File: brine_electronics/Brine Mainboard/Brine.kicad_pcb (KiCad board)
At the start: 2 copper layers, 30.5 x 42.7 mm, 17 parts, among them J1 Conn_01x02_Socket, U1 XIAO-ESP32-S3-SMD, U2 VL53L1CXV0FY1

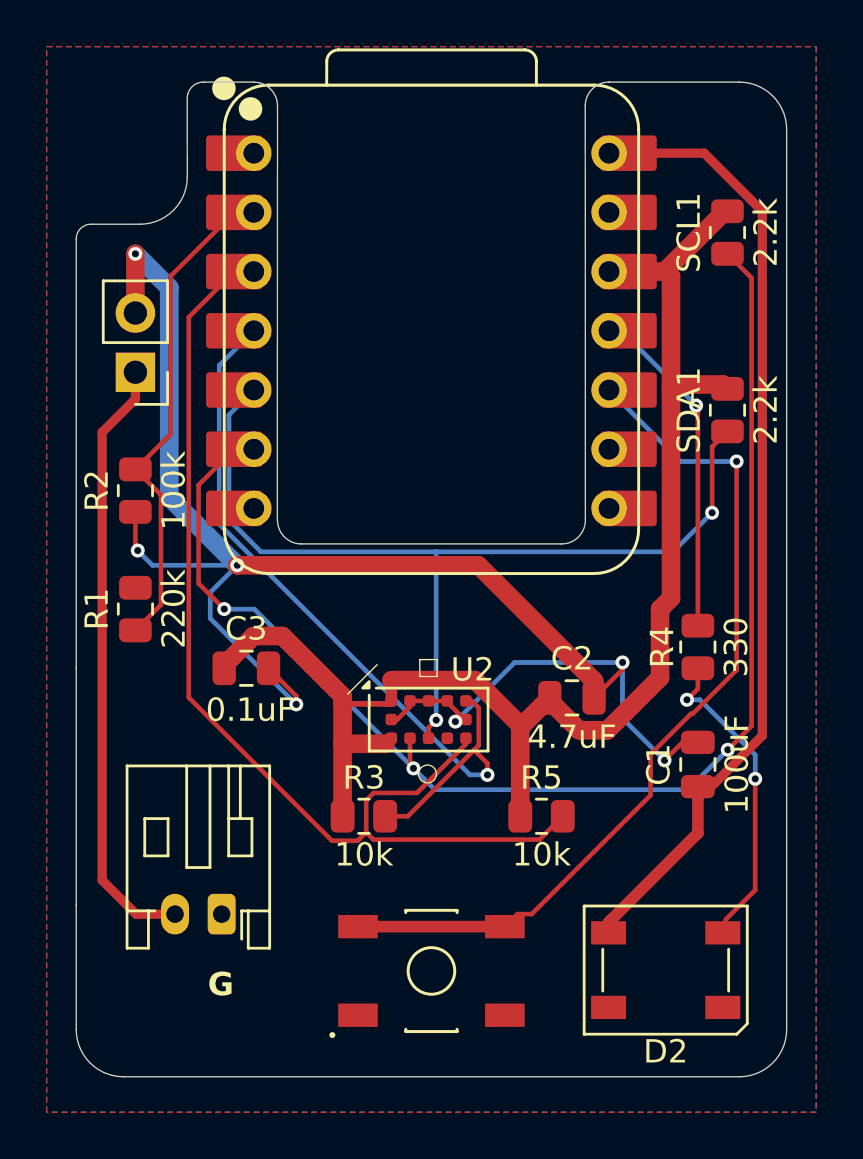
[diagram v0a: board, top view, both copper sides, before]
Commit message: Resolved DRC errors ✅
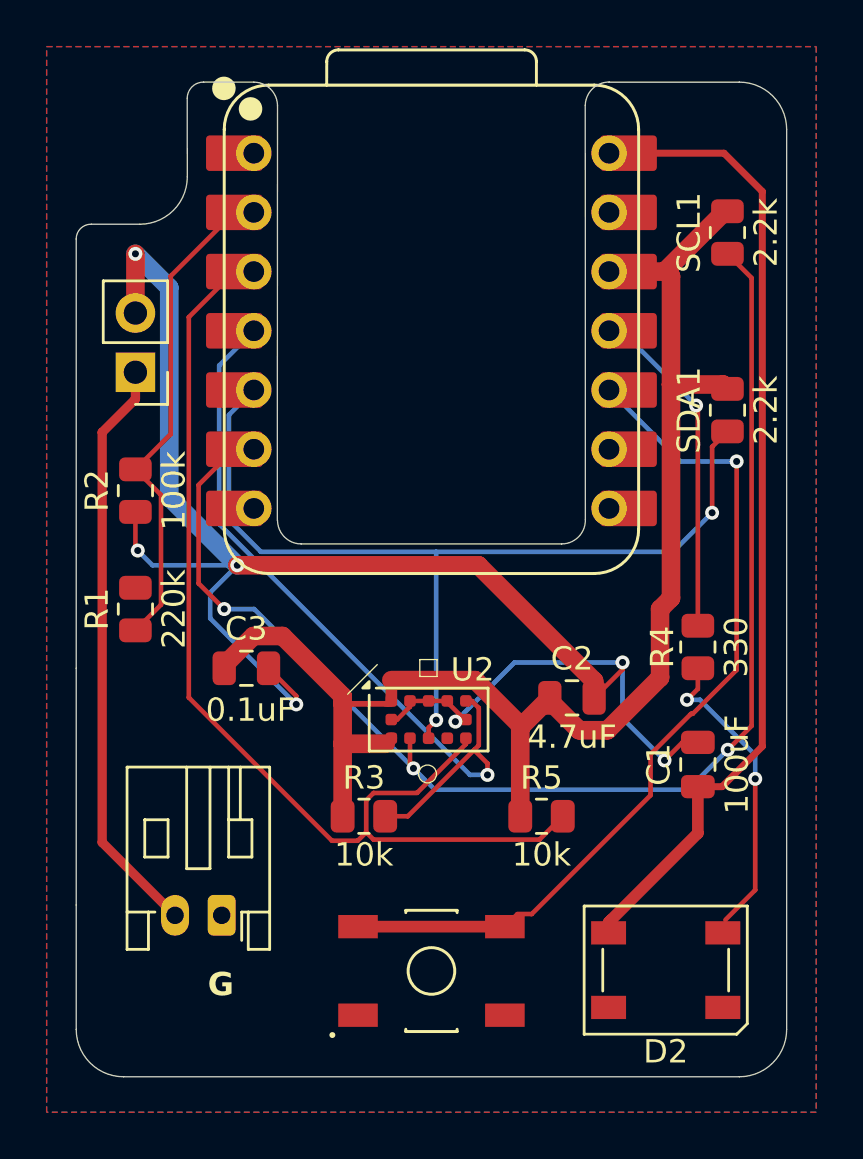
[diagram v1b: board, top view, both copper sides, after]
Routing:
- net /Battery/BATT: track 26.1 -> 25.2 mm
- net +5V: track 41.6 -> 42.4 mm
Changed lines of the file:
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@@
 	(footprint "Connector_JST:JST_PH_S2B-PH-K_1x02_P2.00mm_Horizontal"
 		(layer "F.Cu")
-		(at 143.4 105.8 180)
+		(at 143.4 105.85 180)
 		(descr "JST PH series connector, S2B-PH-K (http://www.jst-mfg.com/product/pdf/eng/ePH.pdf), generated with kicad-footprint-generator")
 		(tags "connector JST PH horizontal")
@@
 	)
 	(segment
-		(start 166.5954 98.1391)
-		(end 164.4045 100.33)
-		(width 0.4)
+		(start 166.5954 74.7954)
+		(end 166.5954 98.6046)
+		(width 0.3)
 		(layer "F.Cu")
 		(net 2)
@@
 	)
 	(segment
-		(start 164.10566 73.152)
-		(end 166.5954 75.64174)
-		(width 0.4)
-		(layer "F.Cu")
-		(net 2)
-	)
-	(segment
 		(start 160 106.156)
 		(end 160.11 106.046)
@@
 	)
 	(segment
-		(start 166.5954 75.64174)
-		(end 166.5954 98.1391)
-		(width 0.4)
+		(start 166.5954 98.6046)
+		(end 164.87 100.33)
+		(width 0.3)
 		(layer "F.Cu")
 		(net 2)
@@
 	)
 	(segment
+		(start 164.87 100.33)
+		(end 164.4045 100.33)
+		(width 0.3)
+		(layer "F.Cu")
+		(net 2)
+	)
+	(segment
+		(start 164.952 73.152)
+		(end 166.5954 74.7954)
+		(width 0.3)
+		(layer "F.Cu")
+		(net 2)
+	)
+	(segment
 		(start 160.855 73.152)
-		(end 164.10566 73.152)
-		(width 0.4)
+		(end 164.952 73.152)
+		(width 0.3)
 		(layer "F.Cu")
 		(net 2)
@@
 	)
 	(segment
-		(start 141.4 105.8)
-		(end 139.7283 105.8)
-		(width 0.4)
-		(layer "F.Cu")
-		(net 8)
-	)
-	(segment
-		(start 138.2724 104.3441)
-		(end 138.2724 85.1293)
-		(width 0.4)
-		(layer "F.Cu")
-		(net 8)
-	)
-	(segment
 		(start 138.2724 85.1293)
 		(end 139.7 83.7017)
@@
 	)
 	(segment
-		(start 139.7283 105.8)
-		(end 138.2724 104.3441)
+		(start 138.2724 102.7224)
+		(end 138.2724 85.1293)
 		(width 0.4)
 		(layer "F.Cu")
+		(net 8)
+	)
+	(segment
+		(start 141.4 105.85)
+		(end 138.2724 102.7224)
+		(width 0.4)
+		(layer "F.Cu")

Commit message: Implemented power latch circuit ⚡
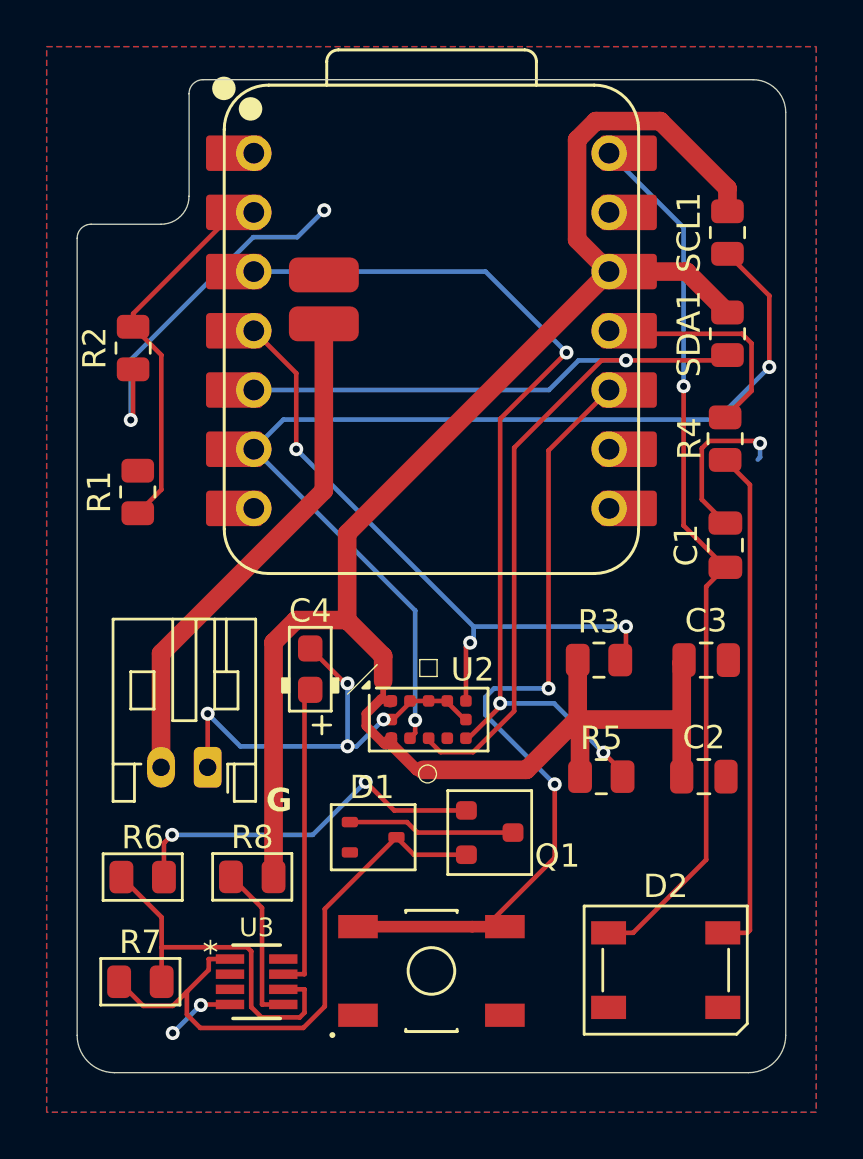
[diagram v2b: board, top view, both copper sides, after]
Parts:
- removed BATT1: Conn_01x02_Pin, Connector_PinHeader_2.54mm:PinHeader_1x02_P2.54mm_Vertical
- added C4: 1.5uF, PCM_Capacitor_Tantalum_SMD_AKL:CP_EIA-2012-12_Kemet-R, F.Cu at (147.2, 95.3)
- added D1: BAT54W, PCM_Package_TO_SOT_SMD_AKL:SOT-323_SC-70, F.Cu at (149.9, 102.5)
- added J2: BATT_CRG_GND, Connector_Wire:SolderWirePad_1x01_SMD_1.5x3mm, F.Cu at (147.8, 78.4)
- added J3: BATT_CRG_GND, Connector_Wire:SolderWirePad_1x01_SMD_1.5x3mm, F.Cu at (147.8, 80.5)
- added Q1: AO3407A, PCM_Package_TO_SOT_SMD_AKL:SOT-23, F.Cu at (154.9, 102.3)
- added R6: 100k, PCM_Resistor_SMD_AKL:R_0805_2012Metric, F.Cu at (140.0, 104.2)
- added R7: 100k, PCM_Resistor_SMD_AKL:R_0805_2012Metric, F.Cu at (139.9, 108.7)
- added R8: 10k, PCM_Resistor_SMD_AKL:R_0805_2012Metric, F.Cu at (144.7, 104.2)
- added U3: LTC2954, LTC2954CTS8_2_TRMPBF:TSOT-23_TS8, F.Cu at (144.9, 108.7)
- J1: value Conn_01x02_Socket -> BATT
- moved C3 19.7 mm to (164.2, 94.9)
- moved R3 12.1 mm to (159.6, 94.9)
- moved C1 9.48 mm to (165.0, 90.0)
- moved R4 9.01 mm to (165.0, 85.4)
- moved C2 6.59 mm to (164.1, 99.9)
- moved J1 6.38 mm to (142.8, 99.5)
- moved R2 6.12 mm to (139.6, 81.5)
- moved R1 5.02 mm to (139.8, 87.7)
- moved SDA1 3.28 mm to (165.1, 80.9)
- moved R5 3.08 mm to (159.7, 99.9)
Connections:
- net /Battery Monitor/BATT renamed /Battery Monitor/SYS_VBAT
- U1 pad 1: unconnected-(U1-GPIO1_A0_D0-Pad1) -> /XIAO ESP32-C3/PWR_INT
- U1 pad 8: unconnected-(U1-GPIO44_D7_RX-Pad8) -> /XIAO ESP32-C3/PWR_KILL
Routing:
- net GND: track 73.5 -> 45.9 mm, vias 7 -> 9
- net /Power Latch/BATT: track 0.00 -> 25.7 mm
- net +3.3V: track 61.9 -> 85.8 mm
- net Net-(Q1-G): track 0.00 -> 16.0 mm, vias 0 -> 2
- net /Power Latch/EN: track 0.00 -> 16.0 mm
- net Net-(U3-PDT): track 0.00 -> 13.2 mm
- net /Distance Sensor/SCL: track 57.8 -> 45.4 mm, vias 3 -> 2
- net Net-(D2-DIN): track 13.1 -> 21.8 mm, vias 2 -> 0
- net /Power Latch/SYS_VBAT: track 0.00 -> 7.19 mm
- net /Power Latch/PWR_INT: track 0.00 -> 6.94 mm
- net /Distance Sensor/XSHUT: track 34.6 -> 28.8 mm, vias 1 -> 3
- net /RGB LED/LED: track 15.4 -> 9.98 mm, vias 1 -> 0
- net /Distance Sensor/GPIO1: track 46.1 -> 40.8 mm, vias 0 -> 3
- net /Battery Monitor/LIFE: track 21.4 -> 16.5 mm
- net /Distance Sensor/SDA: track 40.7 -> 44.1 mm, vias 2 -> 1
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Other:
- board size 30.5 x 42.7 mm -> 30.4 x 42.6 mm

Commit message: Resolved schematic DRC issues ✅
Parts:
- removed S1: TL3342F260QG, TL3342F160QG:SW_TL3342F160QG
- added S2: TS-1187A-B-A-B, TS-1187A:TS1187ABAB, F.Cu at (152.4, 108.3)
- C4: value 1.5uF -> 1uF
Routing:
- net /Button/BUTTON: track 36.8 -> 33.5 mm

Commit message: Updated PCB manufacturing files :mechanical_arm:
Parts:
- added C5: 100uF, Capacitor_SMD:C_0805_2012Metric, F.Cu at (164.2, 101.6)
- added U4: 74AHCT1G125, Package_TO_SOT_SMD:SOT-23-5, F.Cu at (159.7, 102.4)
- J3: value BATT_CRG_GND -> BATT_CRG_BATT
- moved R5 1.66 mm to (159.6, 98.2)
- moved C2 1.64 mm to (164.2, 98.3)
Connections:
- D1 pad 1: /Power Latch/SYS_VBAT -> /Battery Monitor/SYS_VBAT
- D1 pad 3: /Power Latch/BATT -> /Battery/BATT
- Q1 pad 2: /Power Latch/BATT -> /Battery/BATT
- Q1 pad 3: /Power Latch/SYS_VBAT -> /Battery Monitor/SYS_VBAT
- R4 pad 2: /RGB LED/LED -> Net-(R4-Pad2)
- R7 pad 1: /Power Latch/BATT -> /Battery/BATT
- U1 pad 1: /XIAO ESP32-C3/PWR_INT -> /Power Latch/PWR_INT
- U1 pad 8: /XIAO ESP32-C3/PWR_KILL -> /Power Latch/PWR_KILL
- U3 pad 1: /Power Latch/BATT -> /Battery/BATT
- U3 pad 2: /Power Latch/BUTTON -> /Button/BUTTON
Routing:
- net /Power Latch/PWR_INT: track 6.94 -> 70.9 mm, vias 0 -> 2
- net /Power Latch/PWR_KILL: track 0.00 -> 35.9 mm, vias 0 -> 1
- net /Battery Monitor/SYS_VBAT: track 0.00 -> 32.4 mm, vias 0 -> 2
- net /Battery/BATT: track 21.9 -> 53.4 mm, vias 0 -> 1
- net Net-(R4-Pad2): track 0.00 -> 31.0 mm
- net /Power Latch/BATT: track 25.7 -> 0.00 mm
- net GND: track 45.9 -> 67.8 mm, vias 9 -> 12
- net /Button/BUTTON: track 33.5 -> 54.5 mm, vias 2 -> 3
- net +3.3V: track 85.8 -> 66.1 mm, vias 0 -> 2
- net /RGB LED/LED: track 9.98 -> 25.6 mm, vias 0 -> 2
- net /Distance Sensor/XSHUT: track 28.8 -> 41.3 mm, vias 3 -> 2
- net /Power Latch/SYS_VBAT: track 7.19 -> 0.00 mm
- net /Distance Sensor/GPIO1: track 40.8 -> 36.7 mm
- net +5V: track 39.0 -> 42.4 mm
- net /Distance Sensor/SDA: track 44.1 -> 46.4 mm, vias 1 -> 2
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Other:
- board text added: "04/18/26"
- board text removed: "04/03/26"

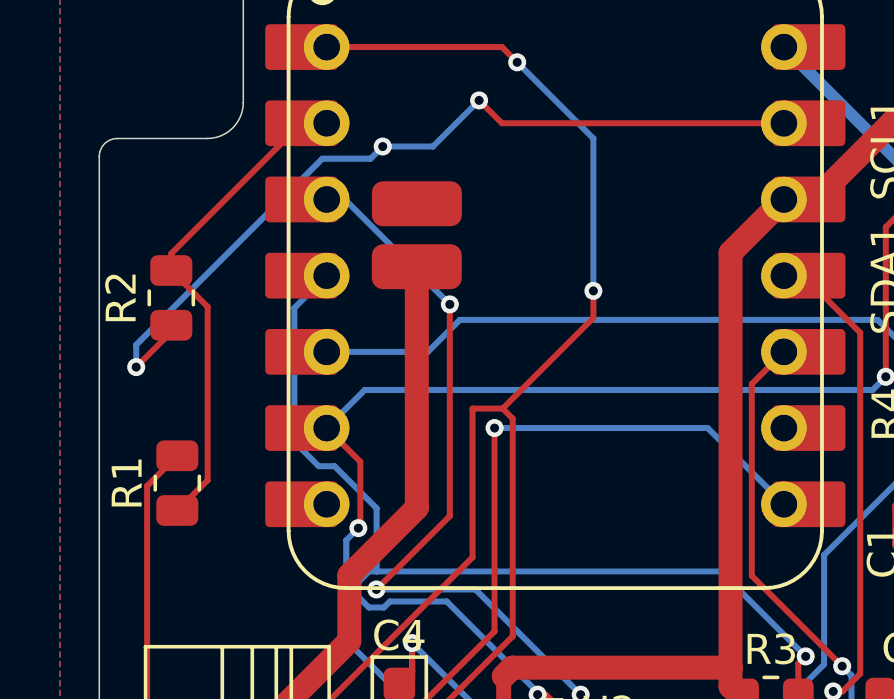
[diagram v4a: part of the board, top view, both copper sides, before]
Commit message: Updated lower latch circuit ⚡
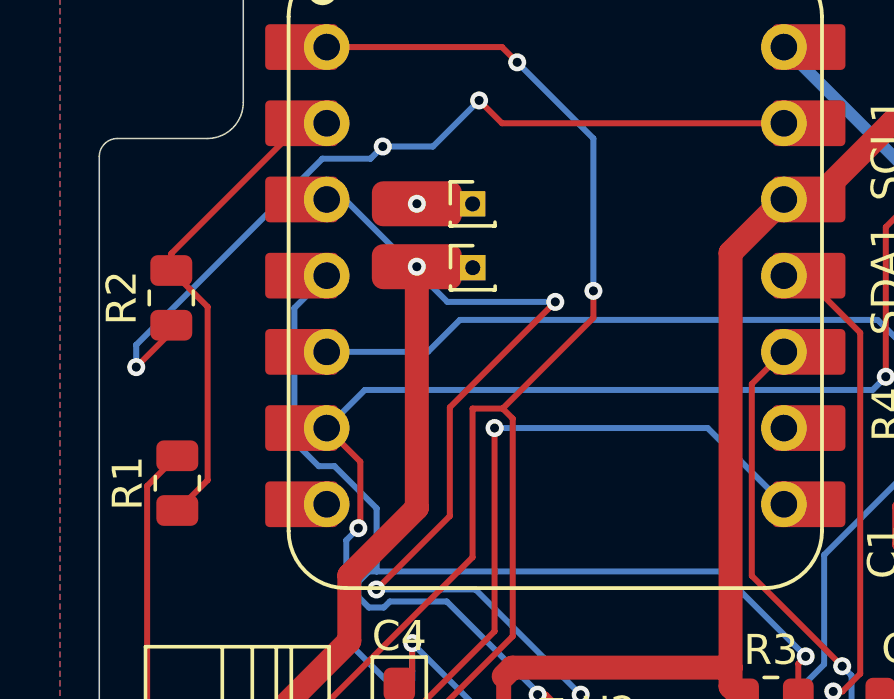
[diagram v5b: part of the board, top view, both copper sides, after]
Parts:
- added J4: BATT_CRG_BATT, Connector_PinHeader_1.00mm:PinHeader_1x01_P1.00mm_Vertical, F.Cu at (149.6, 80.5)
- added J5: BATT_CRG_GND, Connector_PinHeader_1.00mm:PinHeader_1x01_P1.00mm_Vertical, F.Cu at (149.6, 78.4)
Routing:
- net /Distance Sensor/GPIO1: track 36.7 -> 41.7 mm
- net GND: vias 12 -> 13
- net /Battery/BATT: vias 1 -> 2

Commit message: Updated button wiring :bug:
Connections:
- S2 pad B1: /Button/BUTTON -> GND
- S2 pad C1: GND -> /Button/BUTTON
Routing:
- net GND: track 67.8 -> 57.4 mm, vias 13 -> 12
- net /Button/BUTTON: track 54.5 -> 60.5 mm
